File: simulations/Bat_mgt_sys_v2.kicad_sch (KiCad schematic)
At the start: 35 parts, among them Q1 PMOS, Q2 PMOS, U1 TLV76701DRVx, U2 MCP6561-OT, U3 MCP6561-OT, U4 74AHC1G02

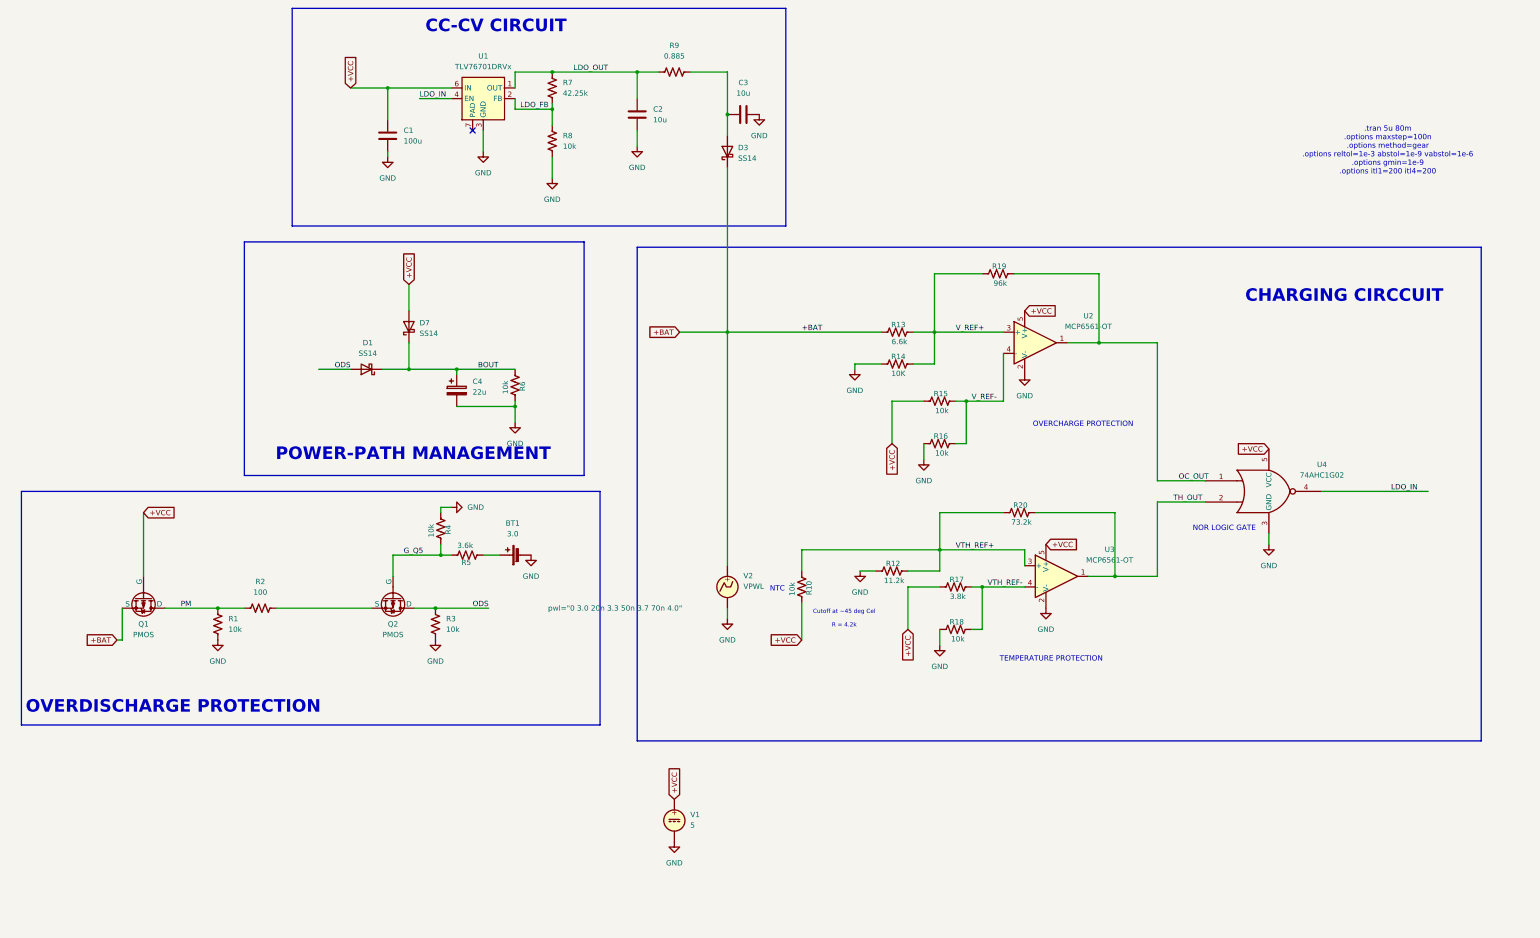
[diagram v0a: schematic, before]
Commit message: trying to figure out sim issue with MCP6561
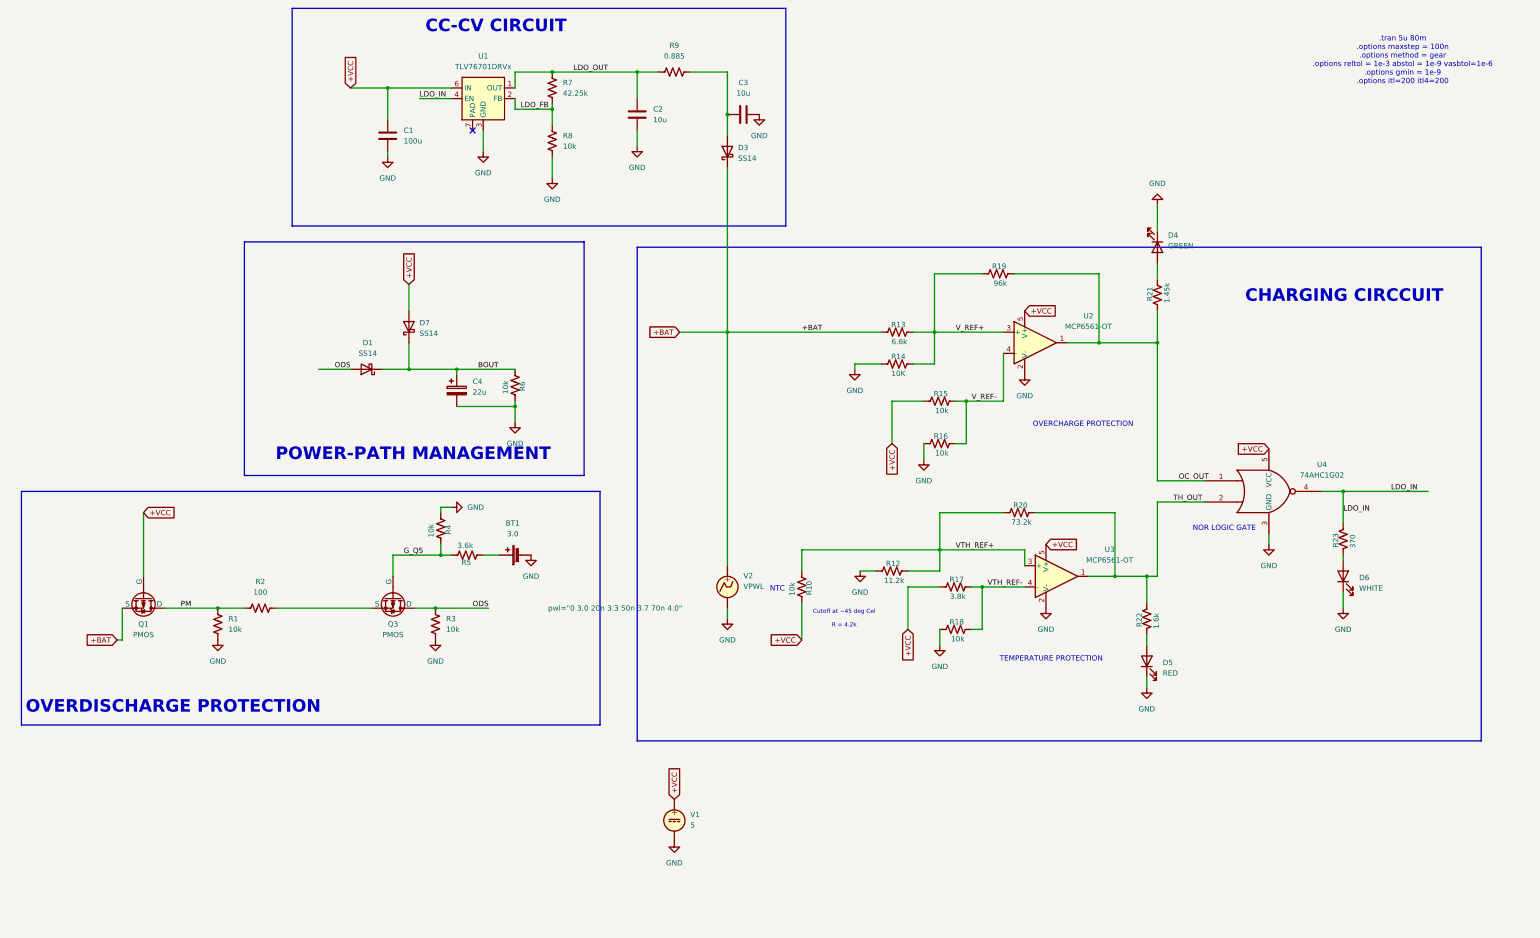
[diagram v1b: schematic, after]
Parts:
- removed Q2: PMOS, symbol Simulation_SPICE:PMOS
- added D4: GREEN, symbol Device:LED
- added D5: RED, symbol Device:LED
- added D6: WHITE, symbol Device:LED
- added Q3: PMOS, symbol Simulation_SPICE:PMOS
- added R21: 1.45k, symbol Device:R_US
- added R22: 1.6k, symbol Device:R_US
- added R23: 370, symbol Device:R_US
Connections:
- net GND: now also D4.1 (K), D5.1 (K), D6.1 (K)
- net G_Q5: now also Q3.2 (G)
- net LDO_IN: now also R23.1
- net OC_OUT: now also R21.1
- net ODS: now also Q3.1 (D)
- net TH_OUT: now also R22.1
- net at R2.1: now also Q3.3 (S)
- new net: D4.2 (A), R21.2
- new net: D5.2 (A), R22.2
- new net: D6.2 (A), R23.2
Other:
- note added: ".tran 5u 80m .options maxstep = 100n .options method = gear .options reltol = 1e-3 abstol = 1e-9 vasbtol=1e-6 .options gmin = 1e-9 .options itl=200 itl4=200"
- note removed: ".tran 5u 80m r .options maxstep=100nr .options method=gearr .options reltol=1e-3 abstol=1e-9 vabstol=1e-6r .options gmin=1e-9r .options itl1=200 itl4=200"

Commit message: simulations fixed with solid model files, results documented
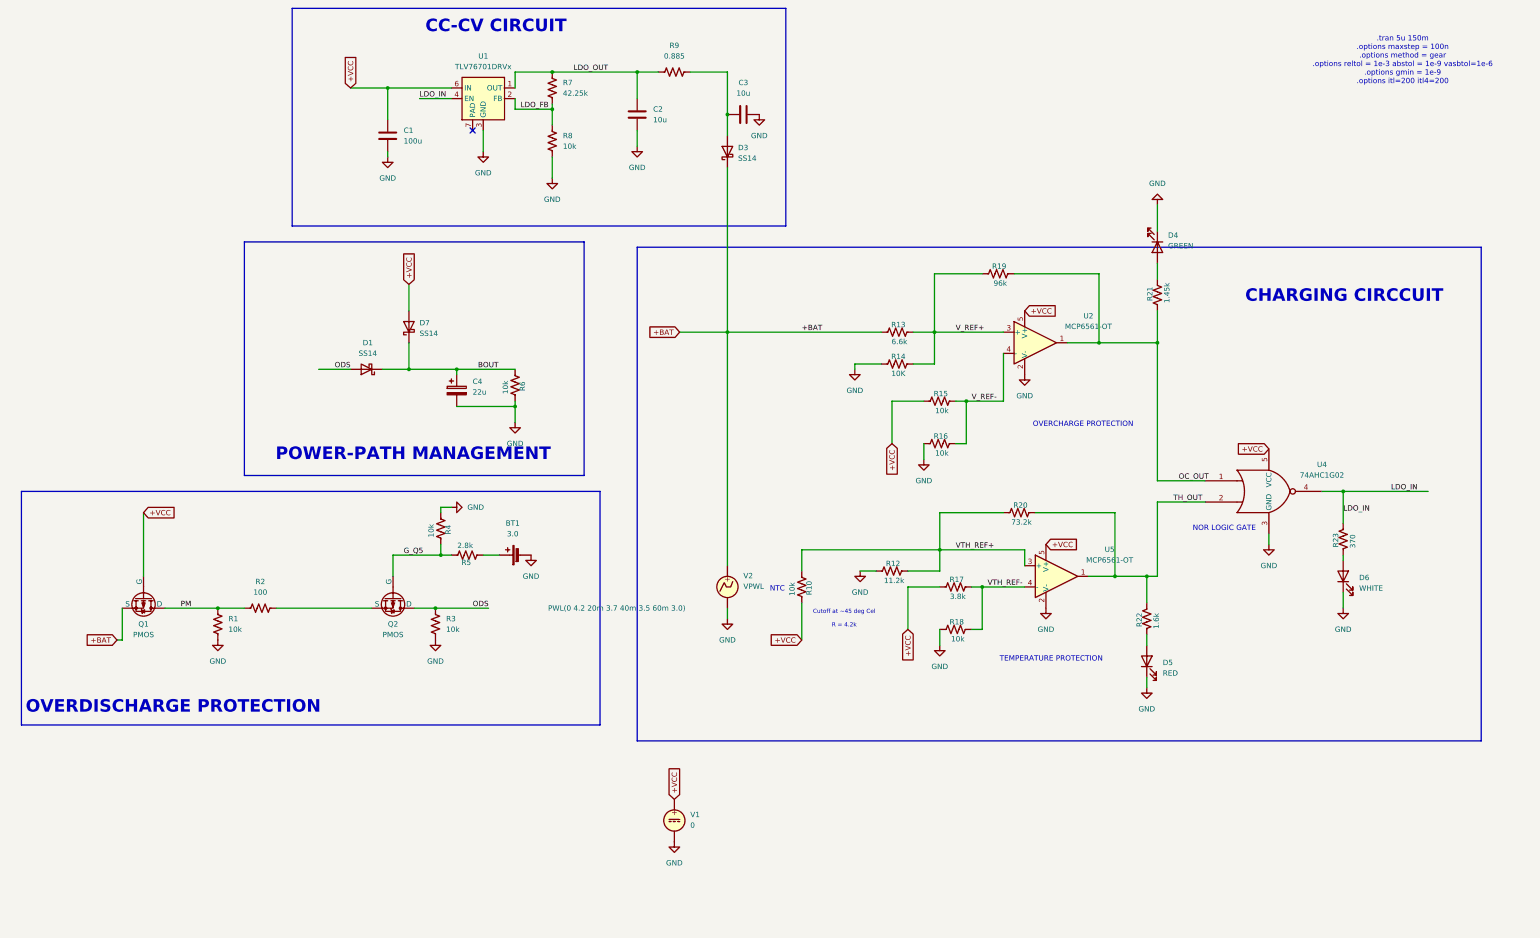
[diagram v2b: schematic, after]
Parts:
- removed Q3: PMOS, symbol Simulation_SPICE:PMOS
- removed U3: MCP6561-OT, Package_TO_SOT_SMD:SOT-23-5, symbol Comparator:MCP6561-OT
- added Q2: PMOS, symbol Simulation_SPICE:PMOS
- added U5: MCP6561-OT, Package_TO_SOT_SMD:SOT-23-5, symbol Comparator:MCP6561-OT
- R5: value 3.6k -> 2.8k
- V1: value 5 -> 0
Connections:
- net +VCC: now also U5.5 (V+)
- net GND: now also U5.2 (V-)
- net G_Q5: now also Q2.2 (G)
- net ODS: now also Q2.1 (D)
- net TH_OUT: now also U5.1
- net VTH_REF+: now also U5.3 (+)
- net VTH_REF-: now also U5.4 (-)
- net at R2.1: now also Q2.3 (S)
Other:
- note added: ".tran 5u 150m .options maxstep = 100n .options method = gear .options reltol = 1e-3 abstol = 1e-9 vasbtol=1e-6 .options gmin = 1e-9 .options itl=200 itl4=200"
- note removed: ".tran 5u 80m .options maxstep = 100n .options method = gear .options reltol = 1e-3 abstol = 1e-9 vasbtol=1e-6 .options gmin = 1e-9 .options itl=200 itl4=200"

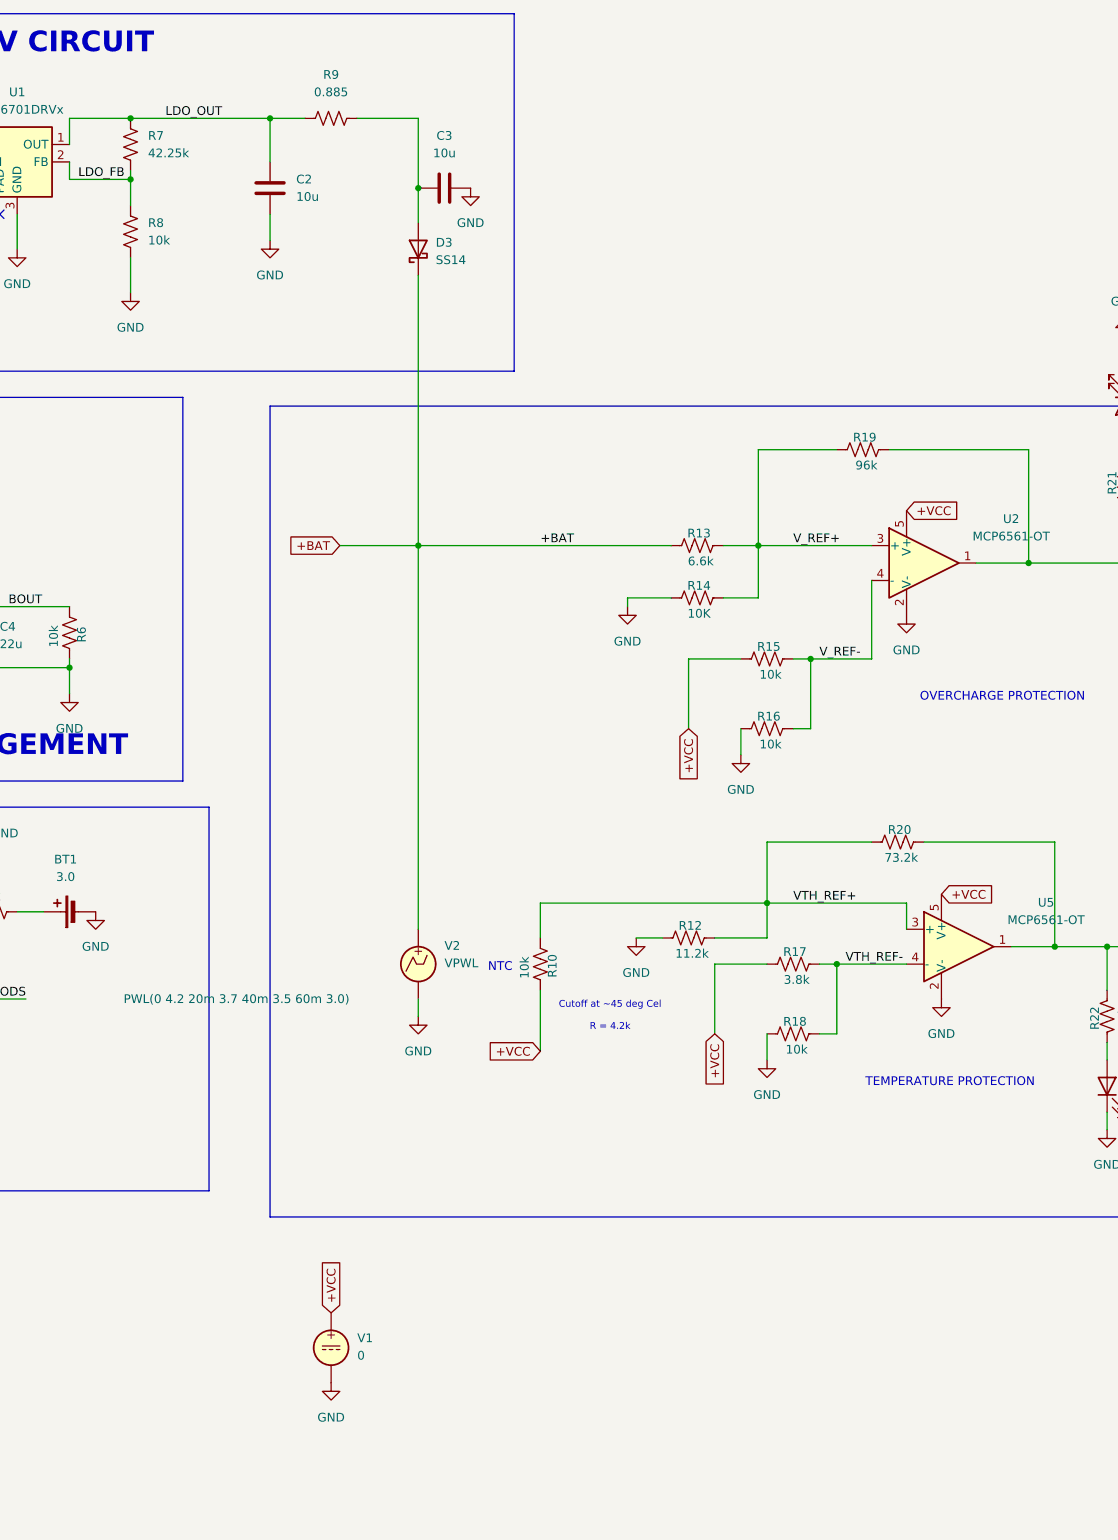
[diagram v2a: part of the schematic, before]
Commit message: updated simulation parameters, and adjusted file locations
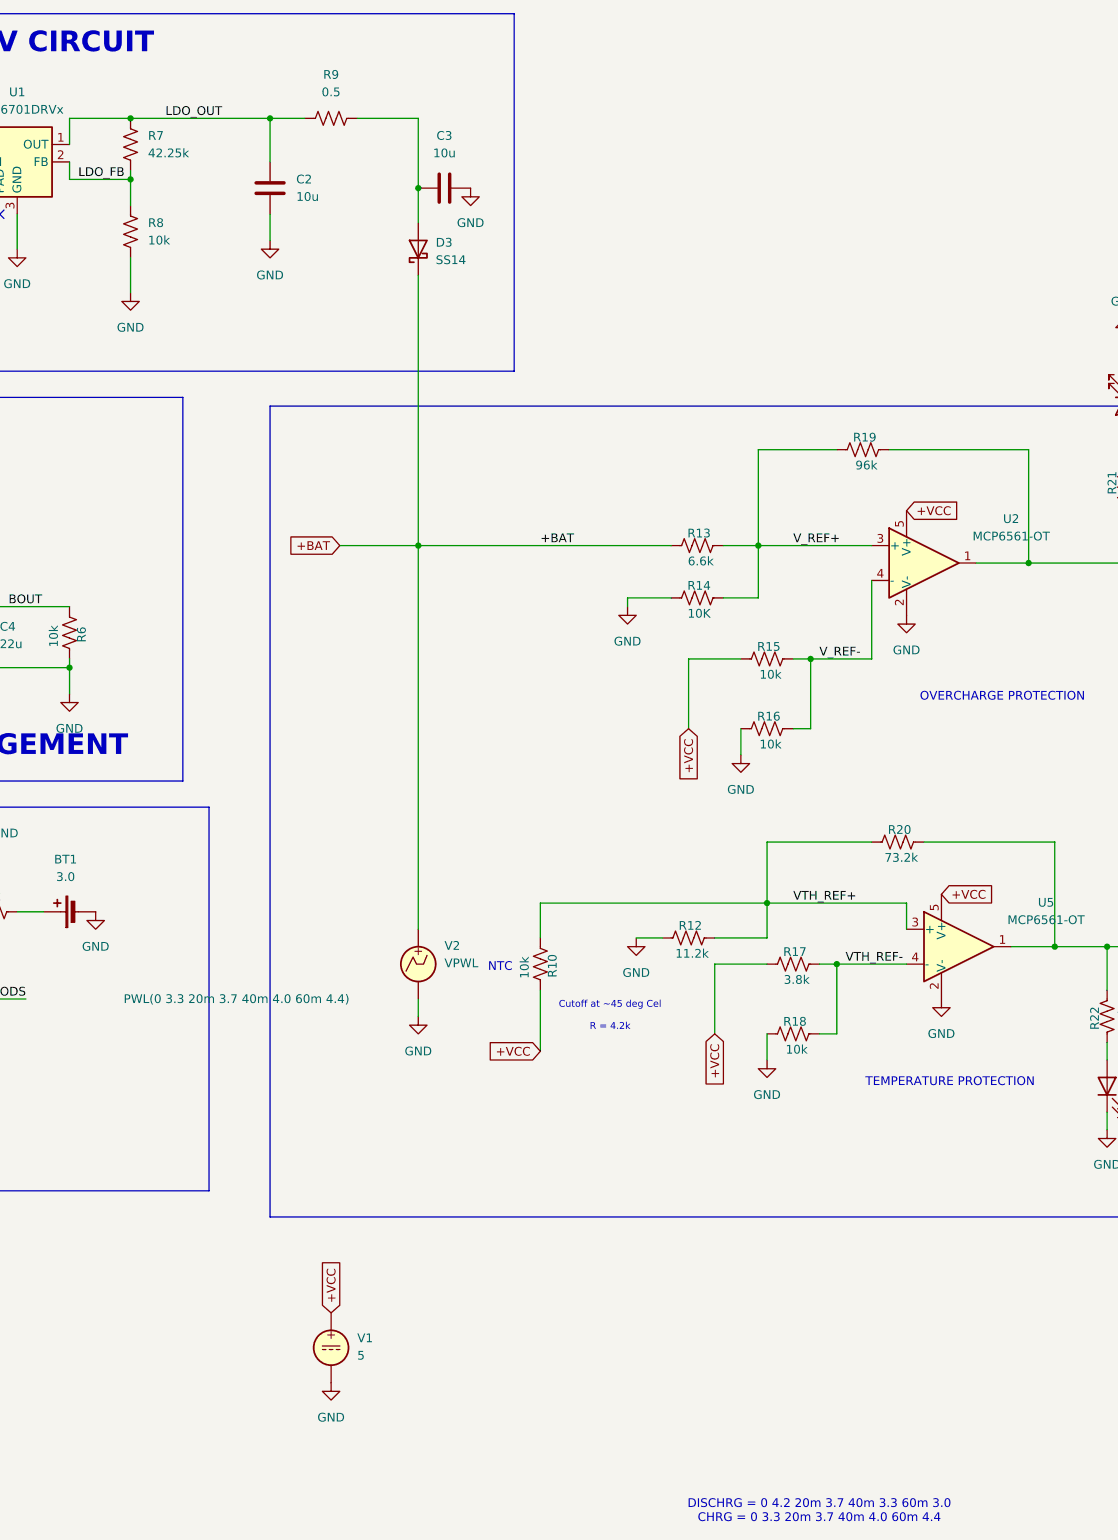
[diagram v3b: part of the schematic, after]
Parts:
- R9: value 0.885 -> 0.5
- V1: value 0 -> 5
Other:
- note added: "DISCHRG = 0 4.2 20m 3.7 40m 3.3 60m 3.0 CHRG = 0 3.3 20m 3.7 40m 4.0 60m 4.4"
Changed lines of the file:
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@@
 		)
 	)
+	(text "DISCHRG = 0 4.2 20m 3.7 40m 3.3 60m 3.0\nCHRG = 0 3.3 20m 3.7 40m 4.0 60m 4.4"
+		(exclude_from_sim no)
+		(at 270.51 251.206 0)
+		(effects
+			(font
+				(size 1.27 1.27)
+			)
+		)
+	)
 	(text ".tran 5u 150m\n.options maxstep = 100n\n.options method = gear\n.options reltol = 1e-3 abstol = 1e-9 vasbtol=1e-6\n.options gmin = 1e-9\n.options itl=200 itl4=200"
 		(exclude_from_sim no)
@@
 			)
 		)
-		(property "Sim.Library" "/home/stanislus/Documents/sim_models/SS14.txt"
+		(property "Sim.Library" "sim_models/SS14.txt"
 			(at 135.89 109.22 0)
 			(hide yes)
@@
 			)
 		)
-		(property "Sim.Library" "/home/stanislus/Documents/KiCAD Projects/BMS-ANAG-T1/sim-PP-MGT/models/BSS215P_L1.lib"
+		(property "Sim.Library" "sim_models/BSS215P_L1.lib"
 			(at 132.08 173.99 0)
 			(hide yes)
@@
 			)
 		)
-		(property "Sim.Library" "/home/stanislus/Documents/KiCAD Projects/BMS-ANAG-T1/sim-OC-SUBCKT/models/MCP6561.txt"
+		(property "Sim.Library" "sim_models/MCP6561.txt"
 			(at 290.83 168.91 0)
 			(hide yes)
@@
 			)
 		)
-		(property "Sim.Params" "PWL(0 4.2 20m 3.7 40m 3.5 60m 3.0)"
+		(property "Sim.Params" "PWL(0 3.3 20m 3.7 40m 4.0 60m 4.4)"
 			(at 169.164 176.53 0)
 			(show_name no)
@@
 			)
 		)
-		(property "Sim.Library" "/home/stanislus/Documents/KiCAD Projects/BMS-ANAG-T1/sim-LDO-SUBCKT/models/TLV76701P_ngspice.lib"
+		(property "Sim.Library" "sim_models/TLV76701P_ngspice.lib"
 			(at 153.67 54.61 0)
 			(hide yes)
@@
 			)
 		)
-		(property "Sim.Library" "/home/stanislus/Documents/KiCAD Projects/BMS-ANAG-T1/sim-PP-MGT/models/BSS215P_L1.lib"
+		(property "Sim.Library" "sim_models/BSS215P_L1.lib"
 			(at 72.39 173.99 0)
 			(hide yes)
@@
 			)
 		)
-		(property "Sim.Library" "/home/stanislus/Documents/KiCAD Projects/BMS-ANAG-T1/sim-OC-SUBCKT/models/NORGATE.txt"
+		(property "Sim.Library" "sim_models/NORGATE.txt"
 			(at 341.63 148.59 0)
 			(hide yes)
@@
 			)
 		)
-		(property "Sim.Library" "/home/stanislus/Documents/sim_models/SS14.txt"
+		(property "Sim.Library" "sim_models/SS14.txt"
 			(at 212.09 67.31 0)
 			(hide yes)
@@
 			)
 		)
-		(property "Value" "0"
+		(property "Value" "5"
 			(at 203.2 228.4701 0)
 			(show_name no)
@@
 			)
 		)
-		(property "Sim.Library" "/home/stanislus/Documents/KiCAD Projects/BMS-ANAG-T1/sim-OC-SUBCKT/models/MCP6561.txt"
+		(property "Sim.Library" "sim_models/MCP6561.txt"
 			(at 285.75 113.03 0)
 			(hide yes)
@@
 			)
 		)
-		(property "Value" "0.885"
+		(property "Value" "0.5"
 			(at 199.39 44.45 90)
 			(show_name no)
@@
 			)
 		)
-		(property "Sim.Library" "/home/stanislus/Documents/sim_models/SS14.txt"
+		(property "Sim.Library" "sim_models/SS14.txt"
 			(at 125.73 119.38 0)
 			(hide yes)
